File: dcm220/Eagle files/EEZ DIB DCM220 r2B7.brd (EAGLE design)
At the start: 155 x 95 mm, 246 parts, among them IC1 Si8662AB-B-IS1, IC10 MC33272ADR2G, IC11 LT3763EFE#PBF, IC12 MC33274ADR2G, IC13 LT3763EFE#PBF, IC2 TPS54060DGQ, IC3 Si8641AB-B-IS1, IC4 M24C32-WMN6P, IC5 LP2985-33DBVR, IC6 74HC2G04GW,125, IC7 N.C., IC8 STM32F373C8T6, IC9 TL431B, J1 4907, J2 571-0500, J3 571-0100, J4 571-0500, J5 571-0100, Q1 BSP716NH6327XTSA1, Q10 BSS84, Q2 NTD5867NLT4G, Q3 NTD5867NLT4G, Q4 BSS205NH6327XTSA1, Q5 BSS84, Q6 BSP716NH6327XTSA1, Q7 NTD5867NLT4G, Q8 NTD5867NLT4G, Q9 BSS205NH6327XTSA1, X1 39-30-1020, X2 77317-104-28LF, X3 N.C., X4 DS1024-2*5R0, Y1 LF XTAL026392

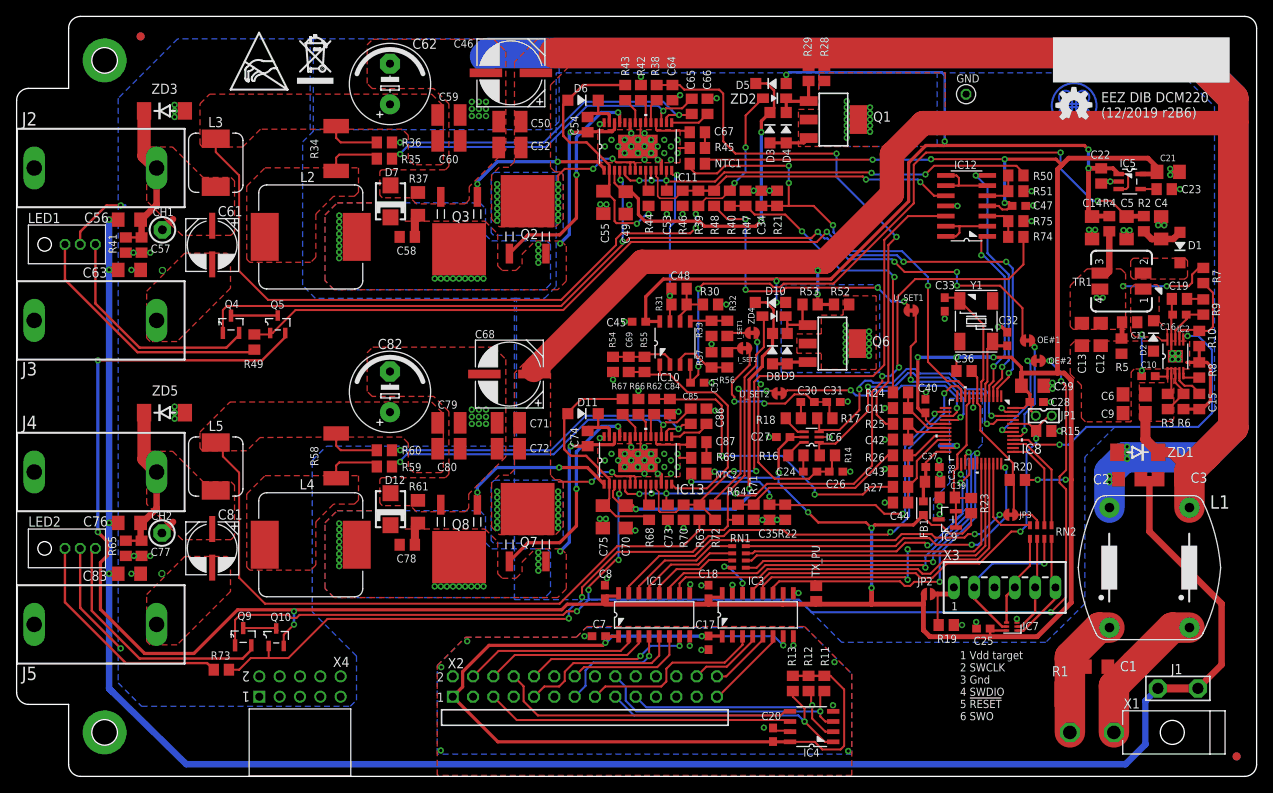
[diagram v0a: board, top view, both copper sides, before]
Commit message: DCP405 EEPROM moved, OSHWA UID added
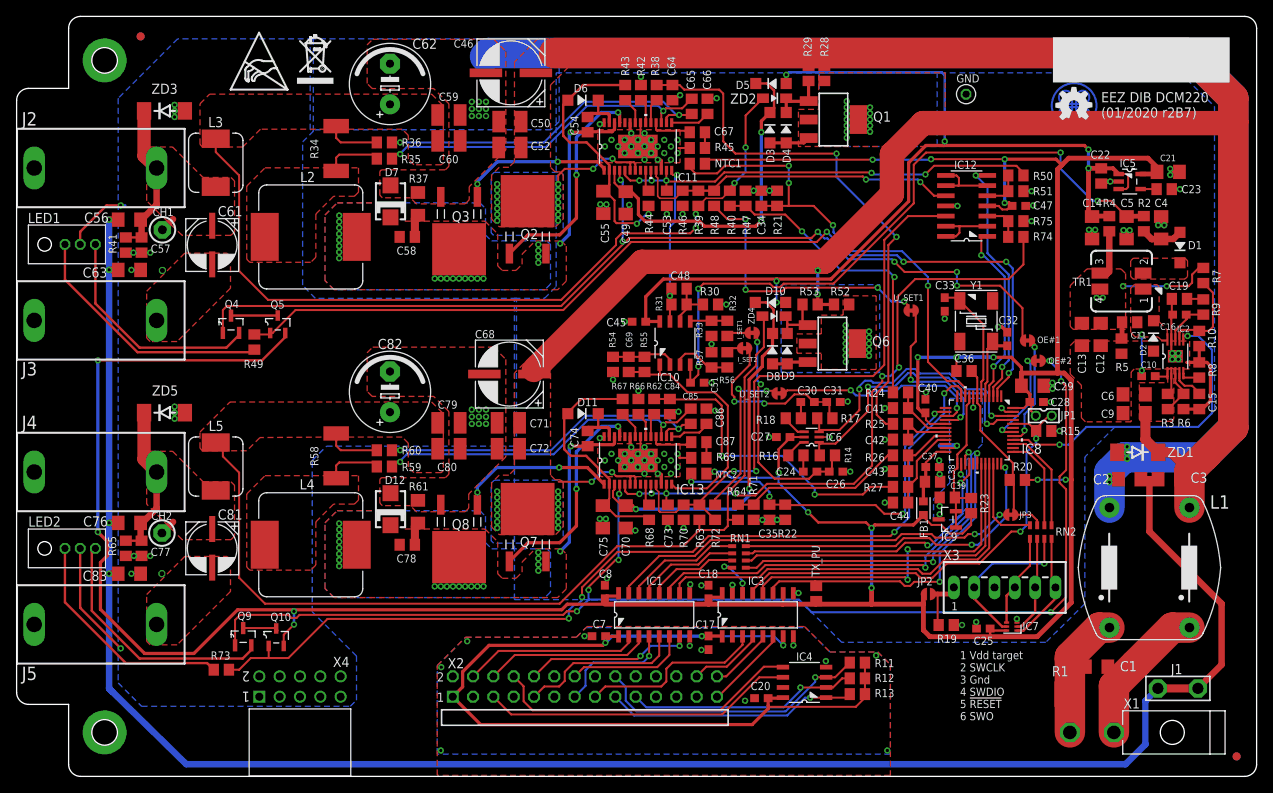
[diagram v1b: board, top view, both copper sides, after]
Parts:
- added U$3: HR000002, OSHWA:CERT-SMALL-SILK
- R45, R69: value 30K -> 100K
- ZD2, ZD4: value MM3Z2V4T1G -> MM3Z9V1T1G
- moved R13 8.17 mm to (105.1, 10.3), turned to 180 degrees
- moved R12 6.13 mm to (105.1, 12.3), turned to 180 degrees
- moved IC4 5.60 mm to (98.5, 11.7)
- moved R11 4.88 mm to (105.1, 14.2), turned to 180 degrees
- moved C20 4.80 mm to (93.1, 9.78), turned to 0 degrees
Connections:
- net N$1 renamed BG1
- net N$15 renamed TG1
- net N$255 renamed TG2
- net N$257 renamed BG2
- removed net DIB_12V: X2.21, X2.22
- removed net DIB_5V: X2.23, X2.24
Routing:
- net V+: track 119.0 -> 114.2 mm
- net DIB_A0: track 34.4 -> 31.4 mm
- net GNDIO: track 2.97 -> 0.16 mm
- net DIB_A2: track 33.7 -> 35.0 mm
- net DIB_SDA: track 37.9 -> 38.8 mm
- net DIB_SCL: track 39.0 -> 39.6 mm
- net DIB_A1: track 29.7 -> 29.0 mm
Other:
- board text added: "EEZ DIB DCM220 (01/2020 r2B7)"
- board text added: "EEZ DIB DCM220 (01/2020 r2B7) Project source code: github.com/eez-open"
- board text removed: "EEZ DIB DCM220 (12/2019 r2B6)"
- board text removed: "EEZ DIB DCM220 (12/2019 r2B6) Project source code: github.com/eez-open"

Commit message: #64
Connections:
- net DIB_BOOT0: now also IC3.7
- net V+: no longer IC3.7
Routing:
- net V+: track 114.2 -> 102.5 mm, vias 3 -> 2
- net DIB_BOOT0: track 9.40 -> 15.3 mm
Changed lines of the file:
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@@
 <layer number="17" name="Pads" color="14" fill="1" visible="yes" active="yes"/>
 <layer number="18" name="Vias" color="6" fill="1" visible="yes" active="yes"/>
-<layer number="19" name="Unrouted" color="6" fill="1" visible="no" active="yes"/>
+<layer number="19" name="Unrouted" color="6" fill="1" visible="yes" active="yes"/>
 <layer number="20" name="Dimension" color="4" fill="1" visible="yes" active="yes"/>
 <layer number="21" name="tPlace" color="7" fill="1" visible="yes" active="yes"/>
@@
 <via x="73.5965" y="16.7005" extent="1-16" drill="0.4" shape="octagon"/>
 <contactref element="X2" pad="1"/>
-<contactref element="IC3" pad="7"/>
 <contactref element="IC3" pad="1"/>
 <contactref element="C17" pad="1"/>
@@
 <wire x1="85.6615" y1="17.526" x2="86.5895" y2="17.526" width="0.4064" layer="1"/>
 <wire x1="86.5895" y1="17.526" x2="86.487" y2="17.5505" width="0.4064" layer="1"/>
-<wire x1="95.8215" y1="17.5006" x2="95.8215" y2="16.383" width="0.254" layer="1"/>
-<via x="95.8215" y="16.383" extent="1-16" drill="0.4" shape="octagon"/>
-<wire x1="94.6785" y1="17.526" x2="85.6615" y2="17.526" width="0.254" layer="16"/>
-<wire x1="94.6785" y1="17.526" x2="95.8215" y2="16.383" width="0.254" layer="16"/>
 <wire x1="86.487" y1="17.5505" x2="88.1516" y2="17.5505" width="0.4064" layer="1"/>
 <wire x1="88.1516" y1="17.5505" x2="88.2015" y2="17.5006" width="0.4064" layer="1"/>
@@
 <wire x1="88.773" y1="13.716" x2="86.216" y2="13.716" width="0.254" layer="1"/>
 <wire x1="86.216" y1="13.716" x2="85" y2="12.5" width="0.254" layer="1"/>
+<contactref element="IC3" pad="7"/>
+<wire x1="92.0115" y1="17.5006" x2="92.0115" y2="18.4785" width="0.254" layer="1"/>
+<wire x1="92.0115" y1="18.4785" x2="92.2655" y2="18.7325" width="0.254" layer="1"/>
+<wire x1="92.2655" y1="18.7325" x2="95.4405" y2="18.7325" width="0.254" layer="1"/>
+<wire x1="95.4405" y1="18.7325" x2="95.8215" y2="18.3515" width="0.254" layer="1"/>
+<wire x1="95.8215" y1="18.3515" x2="95.8215" y2="17.5006" width="0.254" layer="1"/>
 </signal>
 <signal name="N$4">
